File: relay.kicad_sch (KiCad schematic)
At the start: 11 parts, among them K27001 ALFG2PF12, Q27001 DPLS350E

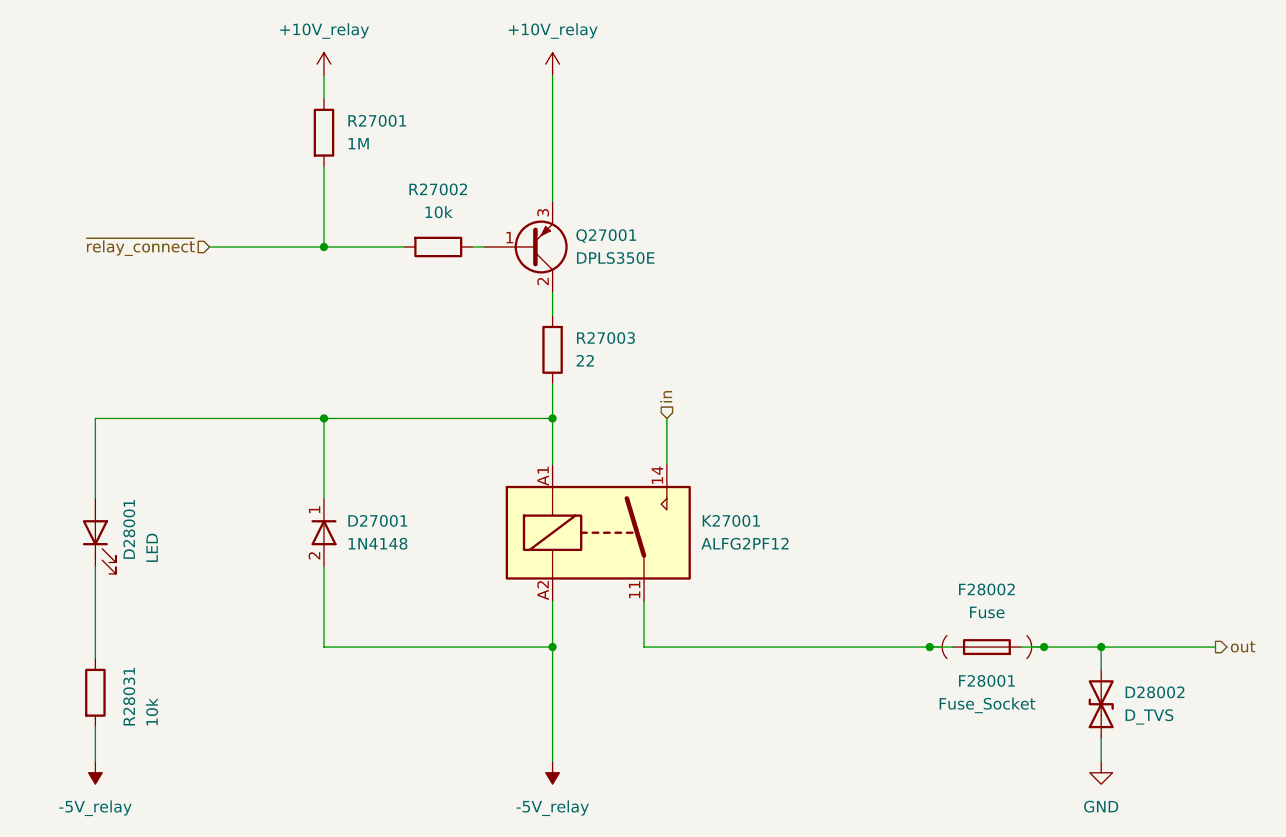
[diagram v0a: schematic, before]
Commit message: add pss 3dmodels and testpoints
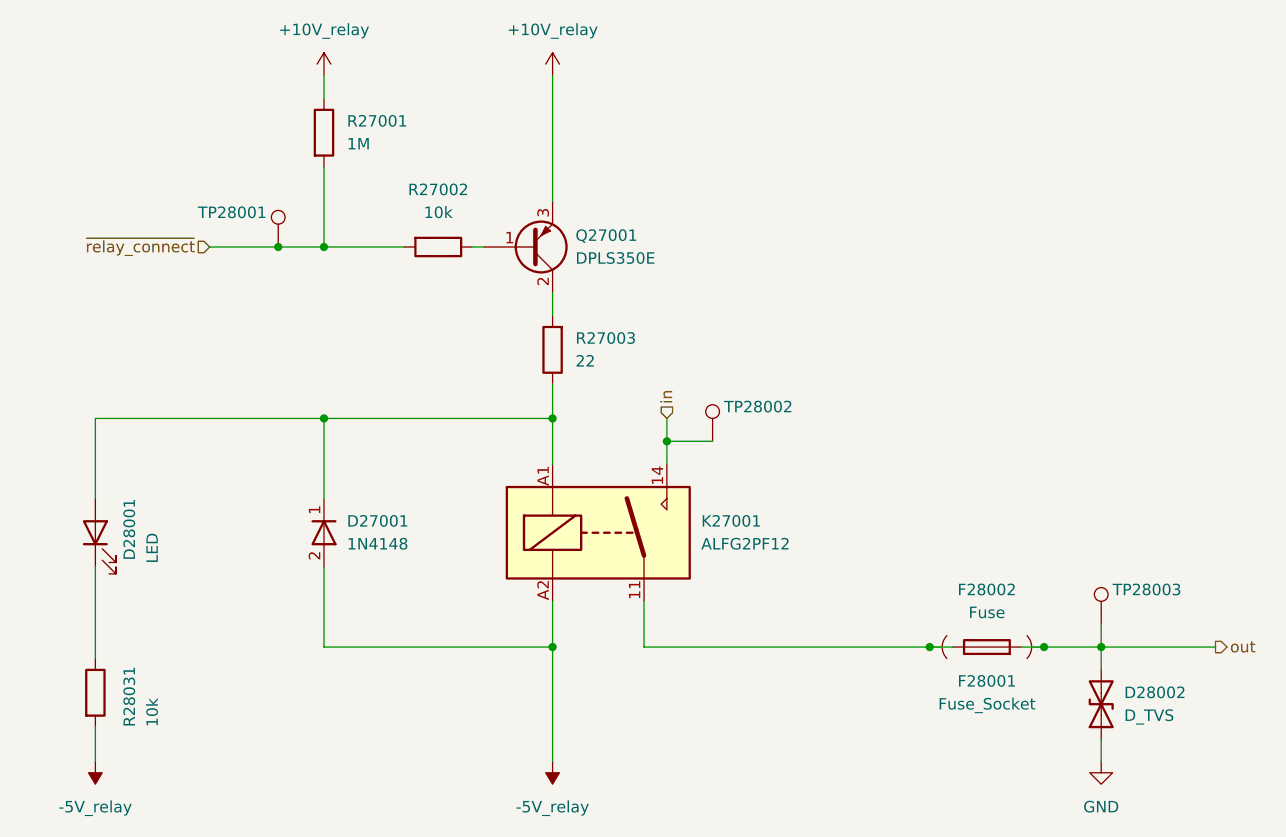
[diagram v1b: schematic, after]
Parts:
- added TP28001, TP28002, TP28003: ~, pss:TP_0805_2012Metric, symbol Connector:TestPoint
- F28001: footprint Fuse:FuseHolder_Blade_ATO_Littelfuse_FLR_178.6165 -> pss:FuseHolder_Blade_ATO_Littelfuse_FLR_178.6165
- K27001: footprint Relay_THT:Relay_SPST_Panasonic_ALFG_FormA_CircularHoles -> pss:Relay_SPST_Panasonic_ALFG_FormA_CircularHoles
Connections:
- net in: now also TP28002.1
- net out: now also TP28003.1
- net ~{relay_connect}: now also TP28001.1

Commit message: edit pss reannotate entire schematic
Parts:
- R27003: MPN RC1210FR-0722RL -> RC1210FR-0722RL
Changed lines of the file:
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@@
 			(project "pss"
 				(path "/3c438cf7-9350-4e9f-8115-1deba8984176/8c067982-1bdd-455d-9e35-2bb5ebdf1fda"
-					(reference "TP28003")
+					(reference "TP3503")
 					(unit 1)
 				)
@@
 			(project "pss"
 				(path "/3c438cf7-9350-4e9f-8115-1deba8984176/8c067982-1bdd-455d-9e35-2bb5ebdf1fda"
-					(reference "#PWR028020")
+					(reference "#PWR03503")
 					(unit 1)
 				)
@@
 			(project "pss"
 				(path "/3c438cf7-9350-4e9f-8115-1deba8984176/8c067982-1bdd-455d-9e35-2bb5ebdf1fda"
-					(reference "D28001")
+					(reference "D3501")
 					(unit 1)
 				)
@@
 			(project "pss"
 				(path "/3c438cf7-9350-4e9f-8115-1deba8984176/8c067982-1bdd-455d-9e35-2bb5ebdf1fda"
-					(reference "D27001")
+					(reference "D3502")
 					(unit 1)
 				)
@@
 			(project "pss"
 				(path "/3c438cf7-9350-4e9f-8115-1deba8984176/8c067982-1bdd-455d-9e35-2bb5ebdf1fda"
-					(reference "R27001")
+					(reference "R3502")
 					(unit 1)
 				)
@@
 			(project "pss"
 				(path "/3c438cf7-9350-4e9f-8115-1deba8984176/8c067982-1bdd-455d-9e35-2bb5ebdf1fda"
-					(reference "#PWR028030")
+					(reference "#PWR03504")
 					(unit 1)
 				)
@@
 			(project "pss"
 				(path "/3c438cf7-9350-4e9f-8115-1deba8984176/8c067982-1bdd-455d-9e35-2bb5ebdf1fda"
-					(reference "K27001")
+					(reference "K3501")
 					(unit 1)
 				)
@@
 			(project "pss"
 				(path "/3c438cf7-9350-4e9f-8115-1deba8984176/8c067982-1bdd-455d-9e35-2bb5ebdf1fda"
-					(reference "#PWR028064")
+					(reference "#PWR03505")
 					(unit 1)
 				)
@@
 			(project "pss"
 				(path "/3c438cf7-9350-4e9f-8115-1deba8984176/8c067982-1bdd-455d-9e35-2bb5ebdf1fda"
-					(reference "D28002")
+					(reference "D3503")
 					(unit 1)
 				)
@@
 			(project "pss"
 				(path "/3c438cf7-9350-4e9f-8115-1deba8984176/8c067982-1bdd-455d-9e35-2bb5ebdf1fda"
-					(reference "#PWR028028")
+					(reference "#PWR03501")
 					(unit 1)
 				)
@@
 			(project "pss"
 				(path "/3c438cf7-9350-4e9f-8115-1deba8984176/8c067982-1bdd-455d-9e35-2bb5ebdf1fda"
-					(reference "TP28001")
+					(reference "TP3501")
 					(unit 1)
 				)
@@
 			(project "pss"
 				(path "/3c438cf7-9350-4e9f-8115-1deba8984176/8c067982-1bdd-455d-9e35-2bb5ebdf1fda"
-					(reference "Q27001")
+					(reference "Q3501")
 					(unit 1)
 				)
@@
 			(project "pss"
 				(path "/3c438cf7-9350-4e9f-8115-1deba8984176/8c067982-1bdd-455d-9e35-2bb5ebdf1fda"
-					(reference "F28001")
+					(reference "F3501")
 					(unit 1)
 				)
@@
 			(project "pss"
 				(path "/3c438cf7-9350-4e9f-8115-1deba8984176/8c067982-1bdd-455d-9e35-2bb5ebdf1fda"
-					(reference "R28031")
+					(reference "R3501")
 					(unit 1)
 				)
@@
 			(project "pss"
 				(path "/3c438cf7-9350-4e9f-8115-1deba8984176/8c067982-1bdd-455d-9e35-2bb5ebdf1fda"
-					(reference "#PWR028019")
+					(reference "#PWR03502")
 					(unit 1)
 				)
@@
 			)
 		)
-		(property "MPN" " RC1210FR-0722RL"
+		(property "MPN" "RC1210FR-0722RL"
 			(at 142.24 93.98 0)
 			(effects
@@
 			(project "pss"
 				(path "/3c438cf7-9350-4e9f-8115-1deba8984176/8c067982-1bdd-455d-9e35-2bb5ebdf1fda"
-					(reference "R27003")
+					(reference "R3504")
 					(unit 1)
 				)
@@
 			(project "pss"
 				(path "/3c438cf7-9350-4e9f-8115-1deba8984176/8c067982-1bdd-455d-9e35-2bb5ebdf1fda"
-					(reference "R27002")
+					(reference "R3503")
 					(unit 1)
 				)
@@
 			(project "pss"
 				(path "/3c438cf7-9350-4e9f-8115-1deba8984176/8c067982-1bdd-455d-9e35-2bb5ebdf1fda"
-					(reference "TP28002")
+					(reference "TP3502")
 					(unit 1)
 				)
@@
 			(project "pss"
 				(path "/3c438cf7-9350-4e9f-8115-1deba8984176/8c067982-1bdd-455d-9e35-2bb5ebdf1fda"
-					(reference "F28002")
-					(unit 1)
-				)
+					(reference "F3502")
+					(unit 1)
+				)

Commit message: edit pss symbol library: export all schematic symbols to library 'pss' and update symbol link
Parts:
- D27001: symbol Device:D -> pss:D
- D28001: symbol Device:LED -> pss:LED
- D28002: symbol Device:D_TVS -> pss:D_TVS
- F28002: symbol Device:Fuse -> pss:Fuse
- K27001: symbol Relay:Panasonic_ALFG2PF12 -> pss:Panasonic_ALFG2PF12
- TP28001, TP28002, TP28003: symbol Connector:TestPoint -> pss:TestPoint
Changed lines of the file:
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@@
 	)
 	(symbol
-		(lib_id "Connector:TestPoint")
+		(lib_id "pss:TestPoint")
 		(at 203.2 124.46 0)
 		(unit 1)
@@
 	)
 	(symbol
-		(lib_id "Device:LED")
+		(lib_id "pss:LED")
 		(at 91.44 114.3 90)
 		(unit 1)
@@
 	)
 	(symbol
-		(lib_id "Device:D")
+		(lib_id "pss:D")
 		(at 116.84 114.3 270)
 		(unit 1)
@@
 	)
 	(symbol
-		(lib_id "Relay:Panasonic_ALFG2PF12")
+		(lib_id "pss:Panasonic_ALFG2PF12")
 		(at 147.32 114.3 0)
 		(unit 1)
@@
 	)
 	(symbol
-		(lib_id "Device:D_TVS")
+		(lib_id "pss:D_TVS")
 		(at 203.2 133.35 90)
 		(unit 1)
@@
 	)
 	(symbol
-		(lib_id "Connector:TestPoint")
+		(lib_id "pss:TestPoint")
 		(at 111.76 82.55 0)
 		(mirror y)
@@
 	)
 	(symbol
-		(lib_id "Connector:TestPoint")
+		(lib_id "pss:TestPoint")
 		(at 160.02 104.14 0)
 		(unit 1)
@@
 	)
 	(symbol
-		(lib_id "Device:Fuse")
+		(lib_id "pss:Fuse")
 		(at 190.5 127 90)
 		(unit 1)

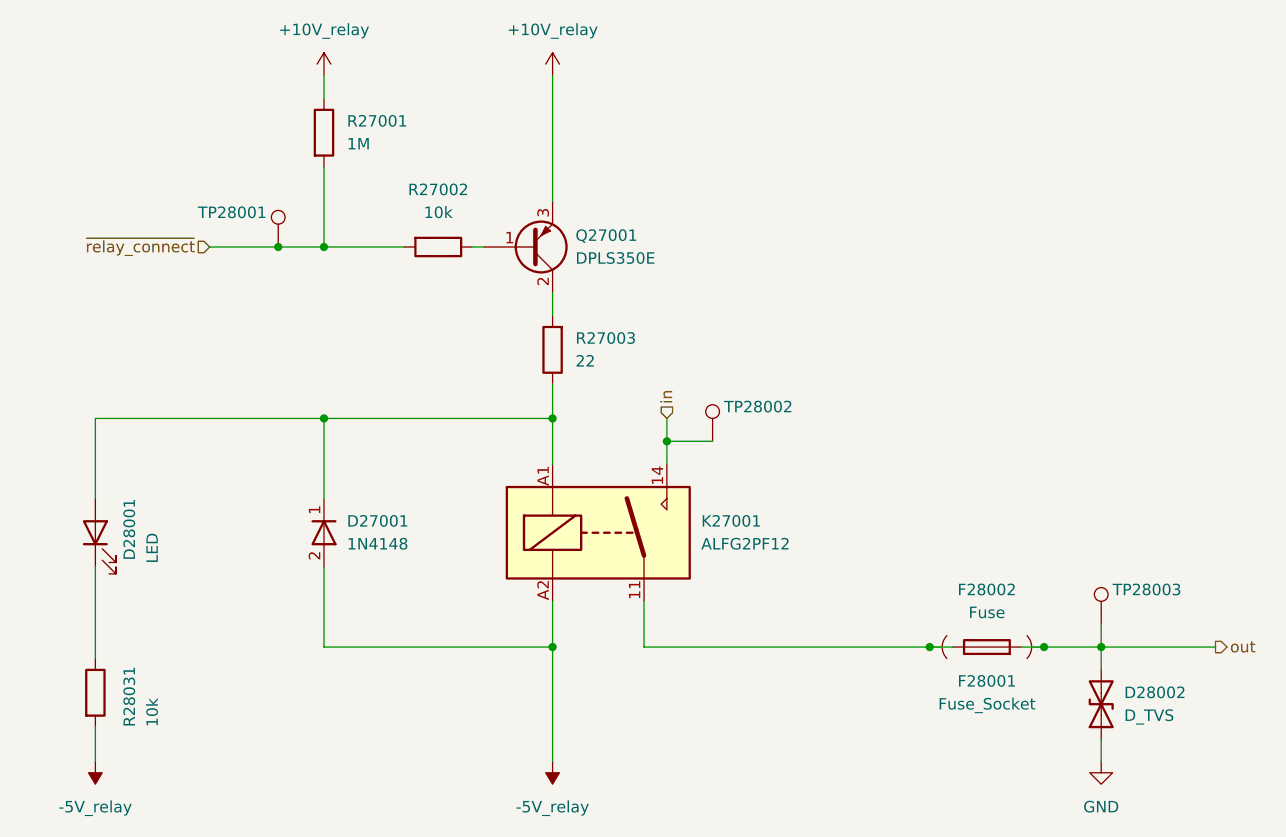
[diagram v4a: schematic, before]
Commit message: edit pss footprint library: export all footprints to library 'pss' and update footprint links
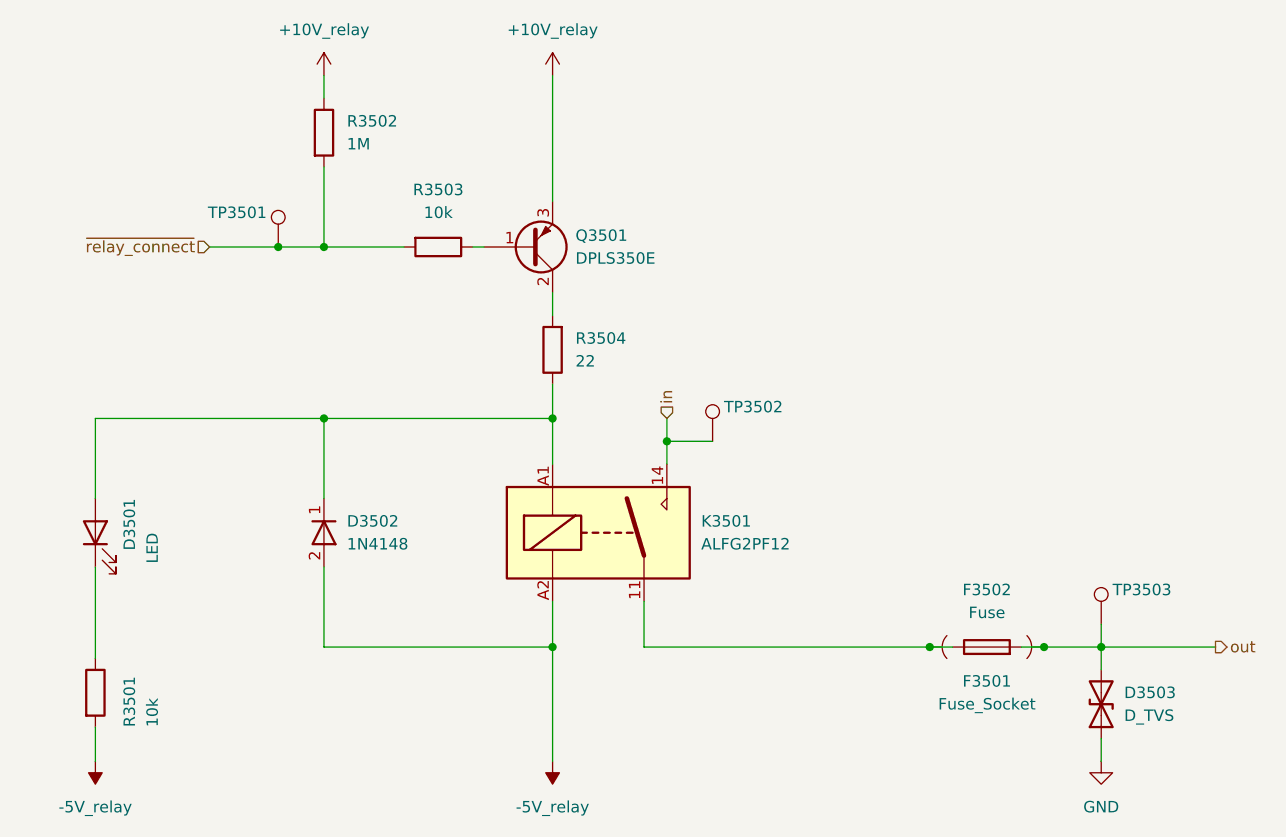
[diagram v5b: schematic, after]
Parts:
- D3501: renamed from D28001; footprint LED_SMD:LED_0805_2012Metric_Pad1.15x1.40mm_HandSolder -> pss:LED_0805_2012Metric_Pad1.15x1.40mm_HandSolder
- D3502: renamed from D27001; footprint Diode_SMD:D_SOD-123 -> pss:D_SOD-123
- D3503: renamed from D28002; footprint Diode_SMD:D_SOD-323_HandSoldering -> pss:D_SOD-323_HandSoldering
- Q3501: renamed from Q27001; footprint Package_TO_SOT_SMD:SOT-223-3_TabPin2 -> pss:SOT-223-3_TabPin2
- R3501: renamed from R28031; footprint Resistor_SMD:R_1210_3225Metric_Pad1.30x2.65mm_HandSolder -> pss:R_1210_3225Metric_Pad1.30x2.65mm_HandSolder
- R3502: renamed from R27001; footprint Resistor_SMD:R_1210_3225Metric_Pad1.30x2.65mm_HandSolder -> pss:R_1210_3225Metric_Pad1.30x2.65mm_HandSolder
- R3503: renamed from R27002; footprint Resistor_SMD:R_1210_3225Metric_Pad1.30x2.65mm_HandSolder -> pss:R_1210_3225Metric_Pad1.30x2.65mm_HandSolder
- R3504: renamed from R27003; footprint Resistor_SMD:R_1210_3225Metric_Pad1.30x2.65mm_HandSolder -> pss:R_1210_3225Metric_Pad1.30x2.65mm_HandSolder
- renumbered F28001 to F3501, F28002 to F3502, K27001 to K3501, TP28001 to TP3501, TP28002 to TP3502, TP28003 to TP3503
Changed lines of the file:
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@@
 		(on_board yes)
 		(dnp no)
-		(property "Reference" "TP28003"
+		(property "Reference" "TP3503"
 			(at 204.47 120.65 0)
 			(effects
@@
 		(dnp no)
 		(fields_autoplaced yes)
-		(property "Reference" "#PWR028020"
+		(property "Reference" "#PWR03503"
 			(at 142.24 67.31 0)
 			(effects
@@
 		(on_board yes)
 		(dnp no)
-		(property "Reference" "D28001"
+		(property "Reference" "D3501"
 			(at 95.25 110.49 0)
 			(effects
@@
 			)
 		)
-		(property "Footprint" "LED_SMD:LED_0805_2012Metric_Pad1.15x1.40mm_HandSolder"
+		(property "Footprint" "pss:LED_0805_2012Metric_Pad1.15x1.40mm_HandSolder"
 			(at 91.44 114.3 0)
 			(effects
@@
 		(dnp no)
 		(fields_autoplaced yes)
-		(property "Reference" "D27001"
+		(property "Reference" "D3502"
 			(at 119.38 113.0299 90)
 			(effects
@@
 			)
 		)
-		(property "Footprint" "Diode_SMD:D_SOD-123"
+		(property "Footprint" "pss:D_SOD-123"
 			(at 116.84 114.3 0)
 			(effects
@@
 		(dnp no)
 		(fields_autoplaced yes)
-		(property "Reference" "R27001"
+		(property "Reference" "R3502"
 			(at 119.38 68.5799 0)
 			(effects
@@
 			)
 		)
-		(property "Footprint" "Resistor_SMD:R_1210_3225Metric_Pad1.30x2.65mm_HandSolder"
+		(property "Footprint" "pss:R_1210_3225Metric_Pad1.30x2.65mm_HandSolder"
 			(at 115.062 69.85 90)
 			(effects
@@
 		(dnp no)
 		(fields_autoplaced yes)
-		(property "Reference" "#PWR028030"
+		(property "Reference" "#PWR03504"
 			(at 142.24 135.89 0)
 			(effects
@@
 		(dnp no)
 		(fields_autoplaced yes)
-		(property "Reference" "K27001"
+		(property "Reference" "K3501"
 			(at 158.75 113.0299 0)
 			(effects
@@
 		(dnp no)
 		(fields_autoplaced yes)
-		(property "Reference" "#PWR028064"
+		(property "Reference" "#PWR03505"
 			(at 203.2 146.05 0)
 			(effects
@@
 		(dnp no)
 		(fields_autoplaced yes)
-		(property "Reference" "D28002"
+		(property "Reference" "D3503"
 			(at 205.74 132.0799 90)
 			(effects
@@
 			)
 		)
-		(property "Footprint" "Diode_SMD:D_SOD-323_HandSoldering"
+		(property "Footprint" "pss:D_SOD-323_HandSoldering"
 			(at 203.2 133.35 0)
 			(effects
@@
 		(dnp no)
 		(fields_autoplaced yes)
-		(property "Reference" "#PWR028028"
+		(property "Reference" "#PWR03501"
 			(at 91.44 135.89 0)
 			(effects
@@
 		(on_board yes)
 		(dnp no)
-		(property "Reference" "TP28001"
+		(property "Reference" "TP3501"
 			(at 110.49 78.74 0)
 			(effects
@@
 		(dnp no)
 		(fields_autoplaced yes)
-		(property "Reference" "Q27001"
+		(property "Reference" "Q3501"
 			(at 144.78 81.2799 0)
 			(effects
@@
 			)
 		)
-		(property "Footprint" "Package_TO_SOT_SMD:SOT-223-3_TabPin2"
+		(property "Footprint" "pss:SOT-223-3_TabPin2"
 			(at 144.78 85.09 0)
 			(effects
@@
 		(on_board yes)
 		(dnp no)
-		(property "Reference" "F28001"
+		(property "Reference" "F3501"
 			(at 190.5 130.81 90)
 			(effects
@@
 		(on_board yes)
 		(dnp no)
-		(property "Reference" "R28031"
+		(property "Reference" "R3501"
 			(at 95.25 135.89 90)
 			(effects
@@
 			)
 		)
-		(property "Footprint" "Resistor_SMD:R_1210_3225Metric_Pad1.30x2.65mm_HandSolder"
+		(property "Footprint" "pss:R_1210_3225Metric_Pad1.30x2.65mm_HandSolder"
 			(at 89.662 132.08 90)
 			(effects
@@
 		(dnp no)
 		(fields_autoplaced yes)
-		(property "Reference" "#PWR028019"
+		(property "Reference" "#PWR03502"
 			(at 116.84 67.31 0)
 			(effects
@@
 		(dnp no)
 		(fields_autoplaced yes)
-		(property "Reference" "R27003"
+		(property "Reference" "R3504"
 			(at 144.78 92.7099 0)
 			(effects
@@
 			)
 		)
-		(property "Footprint" "Resistor_SMD:R_1210_3225Metric_Pad1.30x2.65mm_HandSolder"
+		(property "Footprint" "pss:R_1210_3225Metric_Pad1.30x2.65mm_HandSolder"
 			(at 144.018 93.98 90)
 			(effects
@@
 		(dnp no)
 		(fields_autoplaced yes)
-		(property "Reference" "R27002"
+		(property "Reference" "R3503"
 			(at 129.54 76.2 90)
 			(effects
@@
 			)
 		)
-		(property "Footprint" "Resistor_SMD:R_1210_3225Metric_Pad1.30x2.65mm_HandSolder"
+		(property "Footprint" "pss:R_1210_3225Metric_Pad1.30x2.65mm_HandSolder"
 			(at 129.54 80.772 90)
 			(effects
@@
 		(on_board yes)
 		(dnp no)
-		(property "Reference" "TP28002"
+		(property "Reference" "TP3502"
 			(at 161.29 100.33 0)
 			(effects
@@
 		(dnp no)
 		(fields_autoplaced yes)
-		(property "Reference" "F28002"
+		(property "Reference" "F3502"
 			(at 190.5 120.65 90)
 			(effects
